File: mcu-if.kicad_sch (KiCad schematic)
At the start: 34 parts, among them J10 RJ45_Amphenol_RJMG1BD3B8K1ANR, J8 SD_Card, J9 MCU_USB, U11 KSZ8081RNA

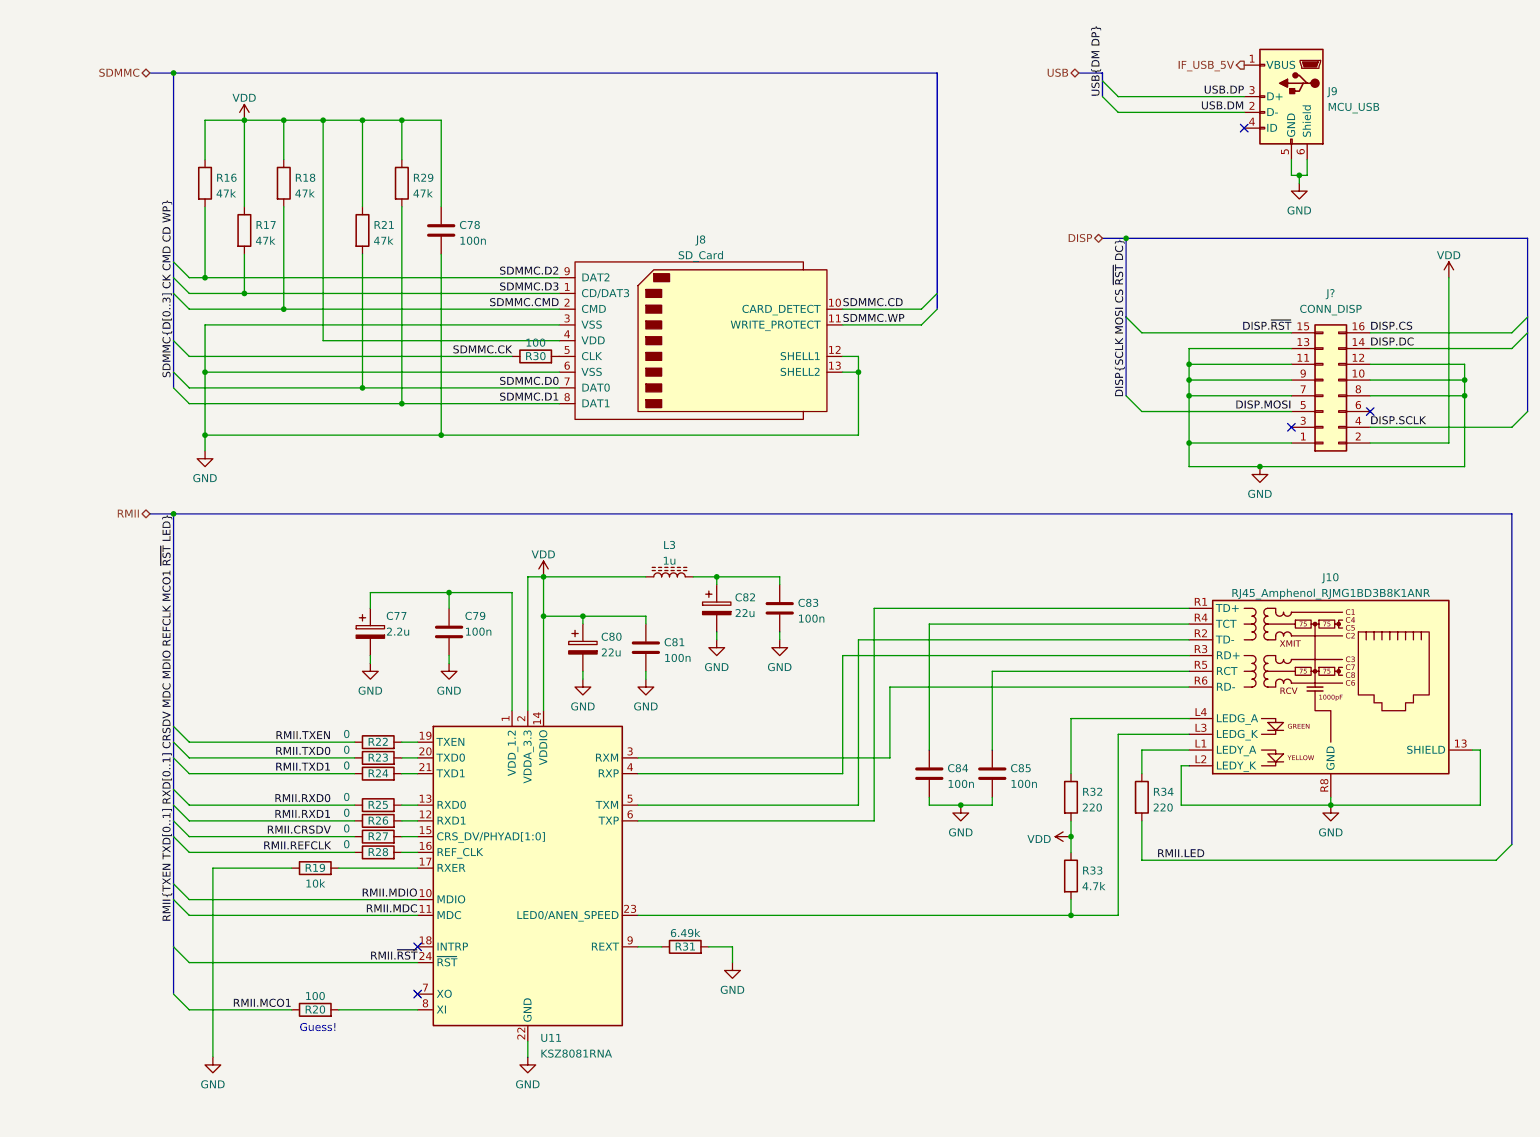
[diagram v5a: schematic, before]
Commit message: Add extension connector, LEDs, buttons
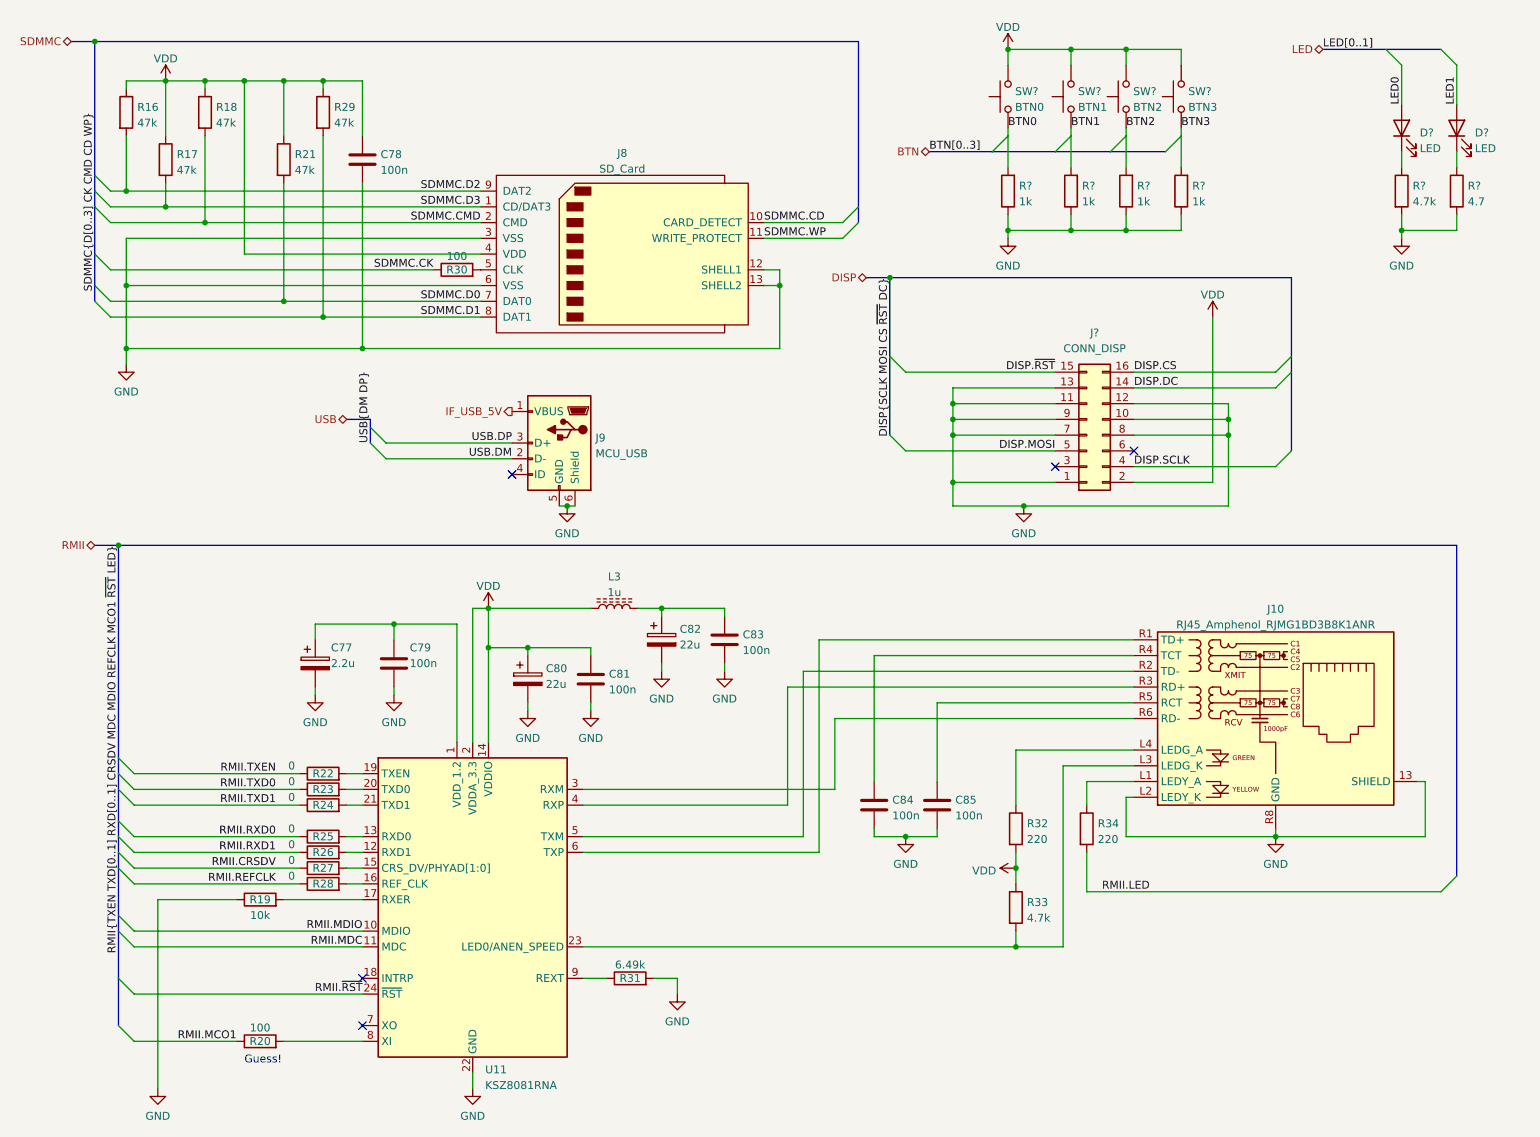
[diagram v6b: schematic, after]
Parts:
- added D? (x2): LED, LED_SMD:LED_PLCC-2_3.4x3.0mm_KA, symbol Device:LED
- added R?: 4.7, symbol Device:R
- added R? (x4): 1k, symbol Device:R
- added R?: 4.7k, symbol Device:R
- added SW?: BTN2, symbol Switch:SW_Push
- added SW?: BTN3, symbol Switch:SW_Push
- added SW?: BTN1, symbol Switch:SW_Push
- added SW?: BTN0, symbol Switch:SW_Push
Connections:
- net GND: now also R?.1, R?.1, R?.1, R?.1, R?.2, R?.2
- net VDD: now also SW?.2, SW?.2, SW?.2, SW?.2
- new net: D?.1 (K), R?.1 (x2)
- new net BTN0: R?.2, SW?.1
- new net BTN1: R?.2, SW?.1
- new net BTN2: R?.2, SW?.1
- new net BTN3: R?.2, SW?.1
- new net LED0: D?.2 (A)
- new net LED1: D?.2 (A)
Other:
- moved on the sheet: C77, C78, C79, C80, C81, C82, C83, C84, C85, J10, J8, J9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

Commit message: Final annotate pass
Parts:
- gave numbers to parts that had none: 13
- renumbered C77 to C501, C78 to C502, C79 to C503, C80 to C504, C81 to C505, C82 to C506, C83 to C507, C84 to C508, C85 to C509, J9 to J501, J8 to J502, J10 to J504, L3 to L501, R16 to R501, R17 to R502, R18 to R503, R19 to R504, R20 to R505, R21 to R506, R29 to R507, R22 to R508, R23 to R509, R24 to R510, R25 to R511, R26 to R512, R27 to R513, R28 to R514, R30 to R515, R31 to R516, R32 to R518, R33 to R519, R34 to R521, U11 to U501
